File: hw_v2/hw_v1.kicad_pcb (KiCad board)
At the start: 4 copper layers, 80.6 x 93.7 mm, 179 parts, among them J1 Conn_02x24_Counter_Clockwise, J14 Conn_01x04, J16 47352-1001, J8 USB_B_Micro, J9 Tag connect, SW1 SW_Push, SW2 SW_Push, U1 MAX9924UAUB_, U10 BMP280, U11 L78M05ABDT-TR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

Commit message: wip CKP/CMP
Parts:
- removed C7: 0.01uF, Capacitor_SMD:C_0805_2012Metric
- removed C8: 4.7nF, Capacitor_SMD:C_0805_2012Metric
- removed the J8 at (115.3, 131.5)
- removed JP11, JP12: Jumper_2_Open, Jumper:SolderJumper-2_P1.3mm_Open_RoundedPad1.0x1.5mm
- removed TP1, TP4: TestPoint, TestPoint:TestPoint_Pad_1.0x1.0mm
- removed U18: VNLD5090, Package_SO:SOIC-8_3.9x4.9mm_P1.27mm
- added R12: 4.7K, Resistor_SMD:R_0603_1608Metric, F.Cu at (185.8, 103.0)
- added R13: 4.7K, Resistor_SMD:R_0603_1608Metric, F.Cu at (185.8, 105.5)
- added R14: 4.7K, Resistor_SMD:R_0603_1608Metric, F.Cu at (185.8, 108.0)
- added R15: 4.7K, Resistor_SMD:R_0603_1608Metric, F.Cu at (185.8, 110.5)
- added R5: 4.7K, Resistor_SMD:R_0603_1608Metric, F.Cu at (185.8, 93.0)
- added R6: 4.7K, Resistor_SMD:R_0603_1608Metric, F.Cu at (185.8, 95.5)
- added R8: 4.7K, Resistor_SMD:R_0603_1608Metric, F.Cu at (185.8, 98.0)
- added R9: 4.7K, Resistor_SMD:R_0603_1608Metric, F.Cu at (185.8, 100.5)
- added RN3: 47k, Resistor_SMD:R_Array_Convex_4x0603, F.Cu at (94.9, 119.8)
- added U2: ~, Package_SO:SOIC-8_3.9x4.9mm_P1.27mm, F.Cu at (131.3, 67.7)
- added U20: ~, Package_SO:SO-8_3.9x4.9mm_P1.27mm, B.Cu at (131.3, 67.7)
- added U3: ~, Package_SO:SOIC-8_3.9x4.9mm_P1.27mm, F.Cu at (138.3, 67.7)
- added U9: TPL7407LAPWR || ULN2003A, Package_SO:TSSOP-16_4.4x5mm_P0.65mm, F.Cu at (202.7, 113.7)
- C1, C2, C68, R2, R3, R7, TP5: moved to B.Cu
- D14, D16: footprint Package_TO_SOT_SMD:SOT-23-6 -> Package_TO_SOT_SMD:SOT-363_SC-70-6
- JP2: moved to F.Cu
- U13: value STM32F407VGTx -> ~; footprint Package_QFP:LQFP-100_14x14mm_P0.5mm -> Package_SO:SO-8_3.9x4.9mm_P1.27mm; moved to B.Cu
- U5: value TPL7407LAPWR -> ~; footprint Package_SO:TSSOP-16_4.4x5mm_P0.65mm -> Package_SO:SO-8_3.9x4.9mm_P1.27mm
- moved J8 151.8 mm to (114.5, 124.6)
- moved U22 139.7 mm to (105.0, 110.0), turned to -45 degrees
- moved U5 119.7 mm to (101.2, 77.2), turned to 90 degrees
- moved U17 102.3 mm to (115.3, 115.0), turned to -135 degrees
- moved R7 98.6 mm to (126.2, 64.8), turned to -90 degrees
- moved TP5 92.0 mm to (120.3, 70.4), turned to 180 degrees
- moved R11 88.9 mm to (119.5, 70.4)
- moved C2 86.5 mm to (123.7, 64.2), turned to -90 degrees
- moved R2 86.3 mm to (121.8, 63.9), turned to -90 degrees
- moved C1 85.7 mm to (122.1, 67.7), turned to -90 degrees
- moved R3 84.0 mm to (124.0, 67.4), turned to -90 degrees
- moved C5 83.3 mm to (125.8, 70.5), turned to -90 degrees
- moved JP3 83.2 mm to (126.1, 69.9), turned to 90 degrees
- moved D19 82.4 mm to (113.4, 117.8), turned to 135 degrees
- moved JP2 78.1 mm to (126.2, 66.4), turned to 90 degrees
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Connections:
- J1 pad 31: FUELPUMP-OUT -> FAN2-OUT
- J1 pad 32: TACHO-OUT -> FUELPUMP-OUT
- J1 pad 33: CAM+ -> TACHO-OUT
- J1 pad 34: unconnected-(J1-Pin_34-Pad34) -> CAM+
- R106 pad 1: /Sensors/AGND -> GND
- R108 pad 1: /Sensors/AGND -> GND
- R57 pad 2: Net-(U18-IN1) -> Net-(U5-IN1)
- R58 pad 1: Net-(U18-IN2) -> Net-(U5-IN2)
- U13 pad 1: /fan2 -> /INY1
- U13 pad 2: /vvt -> unconnected-(U13-STATUS1-Pad2)
- U13 pad 3: /boost -> /INY2
- U13 pad 4: /idle -> unconnected-(U13-STATUS2-Pad4)
- U13 pad 5: unconnected-(U13-PE6-Pad5) -> GND
- U13 pad 6: Net-(BT1-+) -> INJ-2-OUT
- U13 pad 7: 5V_ENABLE -> GND
- U13 pad 8: OSC32_IN -> INJ-1-OUT
- U24 pad 1: (no net) -> unconnected-(U24-Pad1)
- U24 pad 10: (no net) -> unconnected-(U24C-+-Pad10)
- U24 pad 2: (no net) -> unconnected-(U24A---Pad2)
- U24 pad 3: (no net) -> unconnected-(U24A-+-Pad3)
- U24 pad 8: (no net) -> unconnected-(U24-Pad8)
- U24 pad 9: (no net) -> unconnected-(U24C---Pad9)
- U5 pad 1: /fuel_pump -> Net-(U5-IN1)
- U5 pad 2: /fan1 -> unconnected-(U5-STATUS1-Pad2)
- U5 pad 3: /fan2 -> Net-(U5-IN2)
- U5 pad 4: /RPM_OUT -> unconnected-(U5-STATUS2-Pad4)
- U5 pad 5: /RPM_OUT -> GND
- U5 pad 6: /CEL_OUT -> BOOST-OUT
- U5 pad 7: /CEL_OUT -> GND
- U5 pad 8: GND -> IDLE-OUT
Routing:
- net USB_D+: track 0.00 -> 78.4 mm, vias 0 -> 1
- net USB_D-: track 0.00 -> 76.7 mm, vias 0 -> 1
- net GND: track 12.5 -> 32.1 mm, vias 8 -> 14
- net /MAP: track 1.94 -> 17.2 mm
- net /CKP_CMP_Sensors/IN2-: track 0.00 -> 14.3 mm, vias 0 -> 1
- net /IAT: track 2.86 -> 16.3 mm
- net /CLT: track 3.31 -> 16.5 mm
- net VBUS: track 0.00 -> 13.0 mm
- net /TPS: track 2.15 -> 15.1 mm
- net CRANK+: track 0.00 -> 11.1 mm
- net /CKP_CMP_Sensors/IN2+: track 0.00 -> 10.5 mm, vias 0 -> 1
- net +3V3: track 6.93 -> 13.5 mm, vias 0 -> 2
- net Net-(U22-VCAP_2): track 0.00 -> 4.97 mm
- net Net-(U13-VCAP_2): track 4.95 -> 0.00 mm
- net /CKP_CMP_Sensors/CKP_VR: track 0.00 -> 4.66 mm, vias 0 -> 1
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
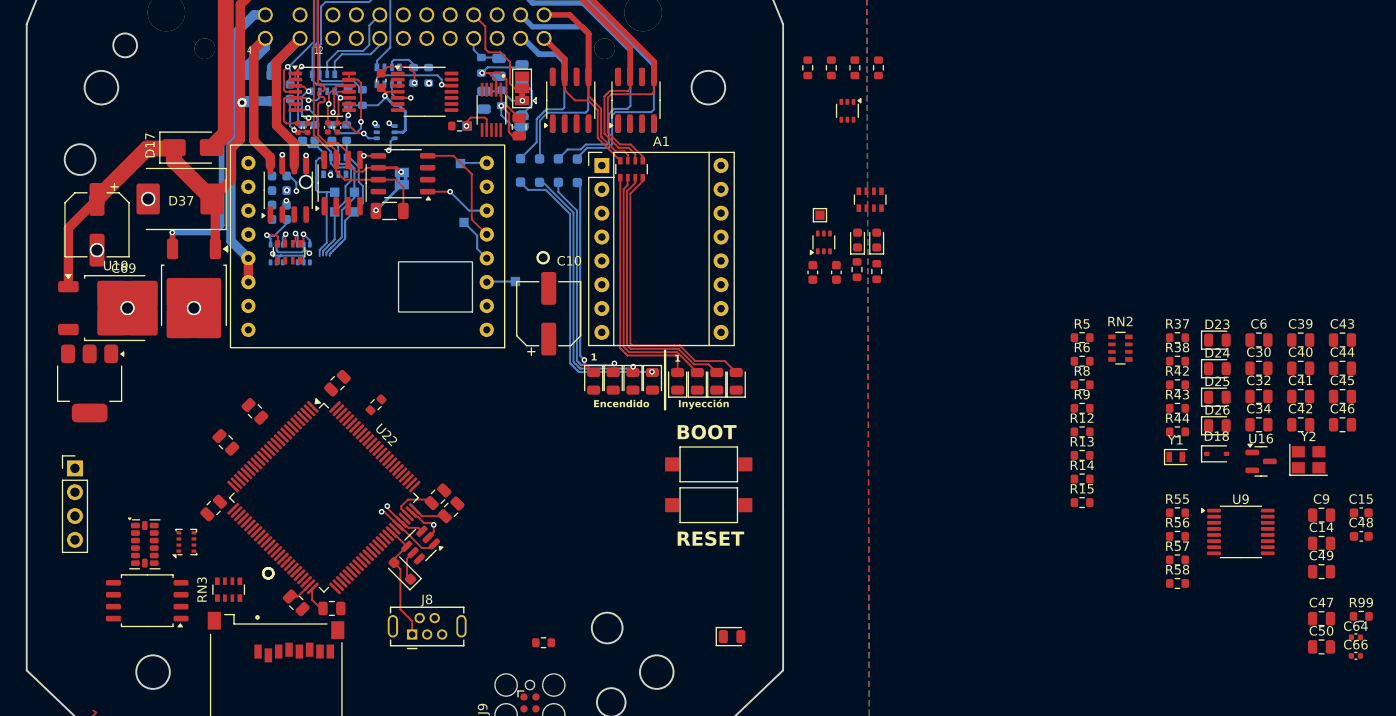
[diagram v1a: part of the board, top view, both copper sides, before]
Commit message: wip routing iny/ign drivers
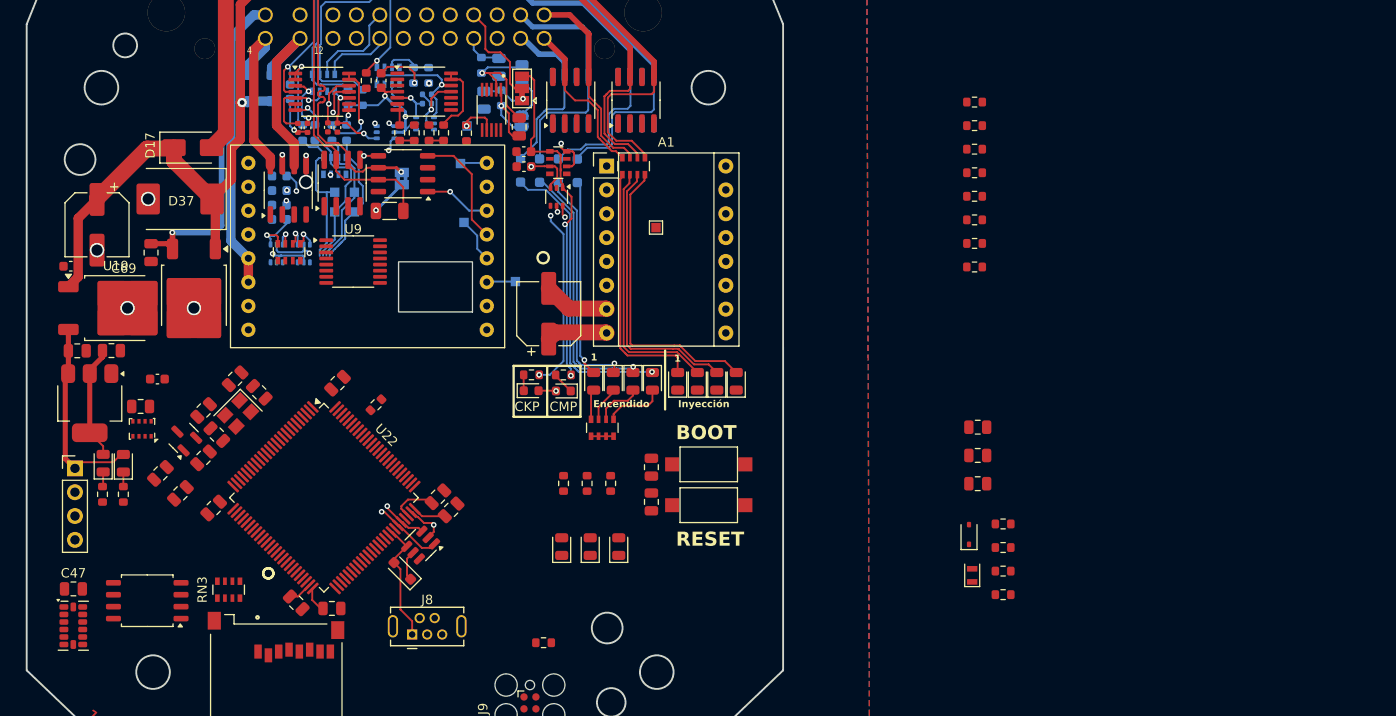
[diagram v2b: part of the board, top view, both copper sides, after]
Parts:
- removed C32: 100nF, Capacitor_SMD:C_0805_2012Metric
- removed C34: 1uF, Capacitor_SMD:C_0805_2012Metric
- C64, C66, D16: moved to B.Cu
- moved C15 140.0 mm to (78.1, 85.3), turned to 180 degrees
- moved C49 134.6 mm to (78.8, 94.3)
- moved C47 133.0 mm to (78.4, 119.7)
- moved C9 130.1 mm to (82.4, 94.3)
- moved C48 129.4 mm to (87.3, 97.4)
- moved C14 128.5 mm to (86.6, 83.9), turned to -90 degrees
- moved C50 128.4 mm to (85.5, 100.3), turned to 180 degrees
- moved C46 126.0 mm to (87.6, 107.4), turned to -135 degrees
- moved C45 124.2 mm to (89.8, 109.5), turned to -135 degrees
- moved C44 121.7 mm to (92.2, 105.8), turned to 45 degrees
- moved R99 120.4 mm to (109.6, 65.6), turned to -90 degrees
- moved C43 120.4 mm to (93.6, 103.3), turned to 135 degrees
- moved D23 119.4 mm to (81.5, 106.3), turned to 90 degrees
- moved R38 115.4 mm to (81.5, 109.6), turned to -90 degrees
- moved C66 115.1 mm to (116.0, 68.0)
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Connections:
- D16 pad 1: unconnected-(D16-Pad1) -> Net-(RN6-R1.2)
- D16 pad 3: Net-(RN6-R1.2) -> unconnected-(D16-Pad3)
- J1 pad 37: STEPPER-B2 -> STEPPER-A2
- J1 pad 38: STEPPER-B1 -> STEPPER-A1
- J1 pad 39: STEPPER-A2 -> STEPPER-B1
- J1 pad 40: STEPPER-A1 -> STEPPER-B2
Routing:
- net +5C: track 90.4 -> 145.6 mm, vias 3 -> 7
- net CAM+: track 0.00 -> 52.3 mm, vias 0 -> 3
- net Net-(JP2-B): track 0.00 -> 37.3 mm, vias 0 -> 2
- net STEPPER-A2: track 0.00 -> 34.4 mm
- net STEPPER-A1: track 0.00 -> 33.2 mm
- net STEPPER-B1: track 0.00 -> 32.4 mm
- net STEPPER-B2: track 0.00 -> 31.4 mm
- net /CKP: track 4.09 -> 25.4 mm, vias 1 -> 2
- net +5V: track 3.26 -> 24.4 mm
- net GND: track 32.1 -> 47.3 mm, vias 14 -> 15
- net +3V3: track 13.5 -> 25.7 mm
- net HEATER+: track 86.8 -> 95.7 mm
- net Net-(U24D--): track 0.00 -> 7.87 mm
- net Net-(D2-A): track 0.00 -> 6.45 mm
- net Net-(D5-A): track 0.00 -> 5.17 mm
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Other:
- board text added: "CKP"
- board text added: "CMP"

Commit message: wip mcu routing
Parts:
- removed JP10, JP9: SolderJumper_3_Bridged12, Jumper:SolderJumper-3_P1.3mm_Bridged2Bar12_Pad1.0x1.5mm
- C40, C41, TP19, U9, Y1: moved to B.Cu
- JP13, JP6, JP7, JP8: moved to F.Cu
- moved JP8 102.2 mm to (144.7, 84.7), turned to 0 degrees
- moved JP6 102.0 mm to (144.7, 89.9), turned to 0 degrees
- moved JP7 101.9 mm to (144.7, 87.3), turned to 0 degrees
- moved C39 90.1 mm to (86.3, 119.9)
- moved R57 84.1 mm to (99.1, 87.2), turned to 90 degrees
- moved D18 83.2 mm to (180.8, 31.0), turned to 0 degrees
- moved R58 82.2 mm to (102.2, 87.2), turned to -90 degrees
- moved R56 81.8 mm to (100.7, 87.2), turned to 90 degrees
- moved C41 79.1 mm to (96.0, 100.8), turned to 135 degrees
- moved Y1 78.7 mm to (97.7, 99.7), turned to -45 degrees
- moved R55 78.0 mm to (103.8, 87.2), turned to -90 degrees
- moved JP13 77.1 mm to (126.2, 77.9), turned to 90 degrees
- moved C40 76.3 mm to (98.8, 98.0), turned to 135 degrees
- moved TP7 68.4 mm to (104.2, 109.4)
- moved TP8 66.4 mm to (102.2, 112.7)
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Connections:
- J1 pad 23: LSU_ip -> LSU_un
- J1 pad 24: LSU_vm -> LSU_rtrim
- J1 pad 25: LSU_rtrim -> unconnected-(J1-Pin_25-Pad25)
- J1 pad 26: LSU_un -> unconnected-(J1-Pin_26-Pad26)
- J1 pad 27: unconnected-(J1-Pin_27-Pad27) -> LSU_vm
- J1 pad 28: unconnected-(J1-Pin_28-Pad28) -> LSU_ip
- J14 pad 3: Net-(J14-Pin_3) -> USART_2_RX
- J14 pad 4: Net-(J14-Pin_4) -> USART_2_TX
- U22 pad 1: /fan1 -> /fan2
- U22 pad 15: /CEL_OUT -> unconnected-(U22-PC0-Pad15)
- U22 pad 2: /fuel_pump -> /fan1
- U22 pad 23: /IAT -> /CLT
- U22 pad 26: /CLT -> /IAT
- U22 pad 3: /fan2 -> /fuel_pump
- U22 pad 42: /RPM_OUT -> unconnected-(U22-PE11-Pad42)
- U22 pad 92: unconnected-(U22-PB6-Pad92) -> /RPM_OUT
- U22 pad 93: unconnected-(U22-PB7-Pad93) -> /CEL_OUT
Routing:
- net /O2: track 1.55 -> 54.5 mm, vias 0 -> 2
- net /VBATT: track 1.55 -> 51.8 mm, vias 0 -> 2
- net IGN_V+: track 0.00 -> 39.0 mm, vias 0 -> 3
- net LSU_vm: track 0.00 -> 37.0 mm
- net LSU_ip: track 0.00 -> 36.9 mm
- net /MAP: track 17.2 -> 52.9 mm, vias 0 -> 1
- net /TPS: track 15.1 -> 50.4 mm, vias 0 -> 1
- net /IAT: track 16.3 -> 51.6 mm, vias 0 -> 1
- net /fuel_pump: track 0.00 -> 33.1 mm, vias 0 -> 1
- net /fan1: track 0.00 -> 32.3 mm, vias 0 -> 1
- net /fan2: track 0.00 -> 31.6 mm, vias 0 -> 1
- net FAN-OUT: track 0.00 -> 31.1 mm, vias 0 -> 2
- net LSU_rtrim: track 0.00 -> 30.7 mm
- net /CLT: track 16.5 -> 47.1 mm, vias 0 -> 1
- net TACHO-OUT: track 0.00 -> 30.5 mm, vias 0 -> 2
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
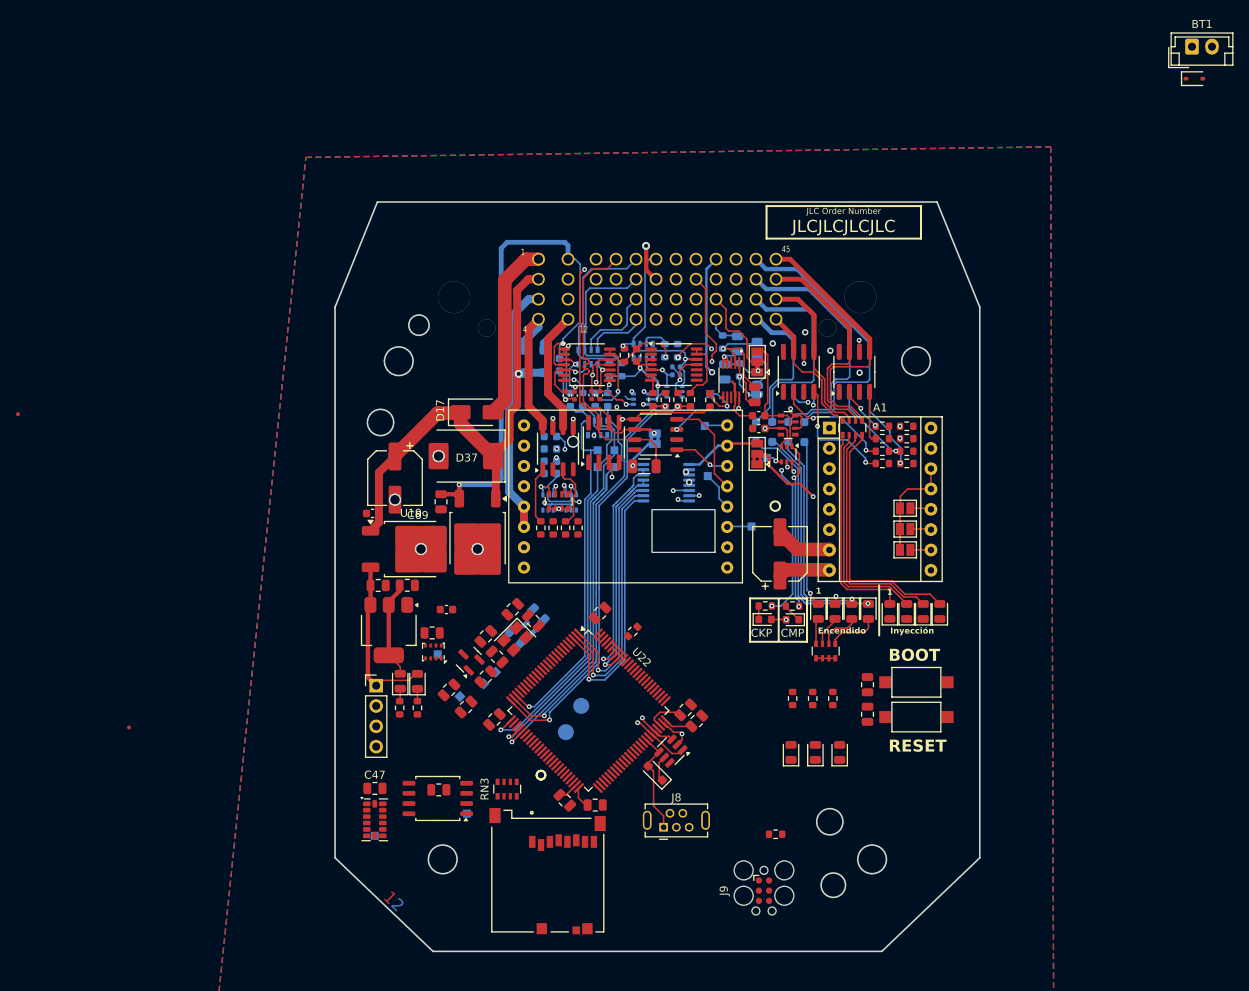
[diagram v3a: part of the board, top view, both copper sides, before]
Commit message: update ADC oamp
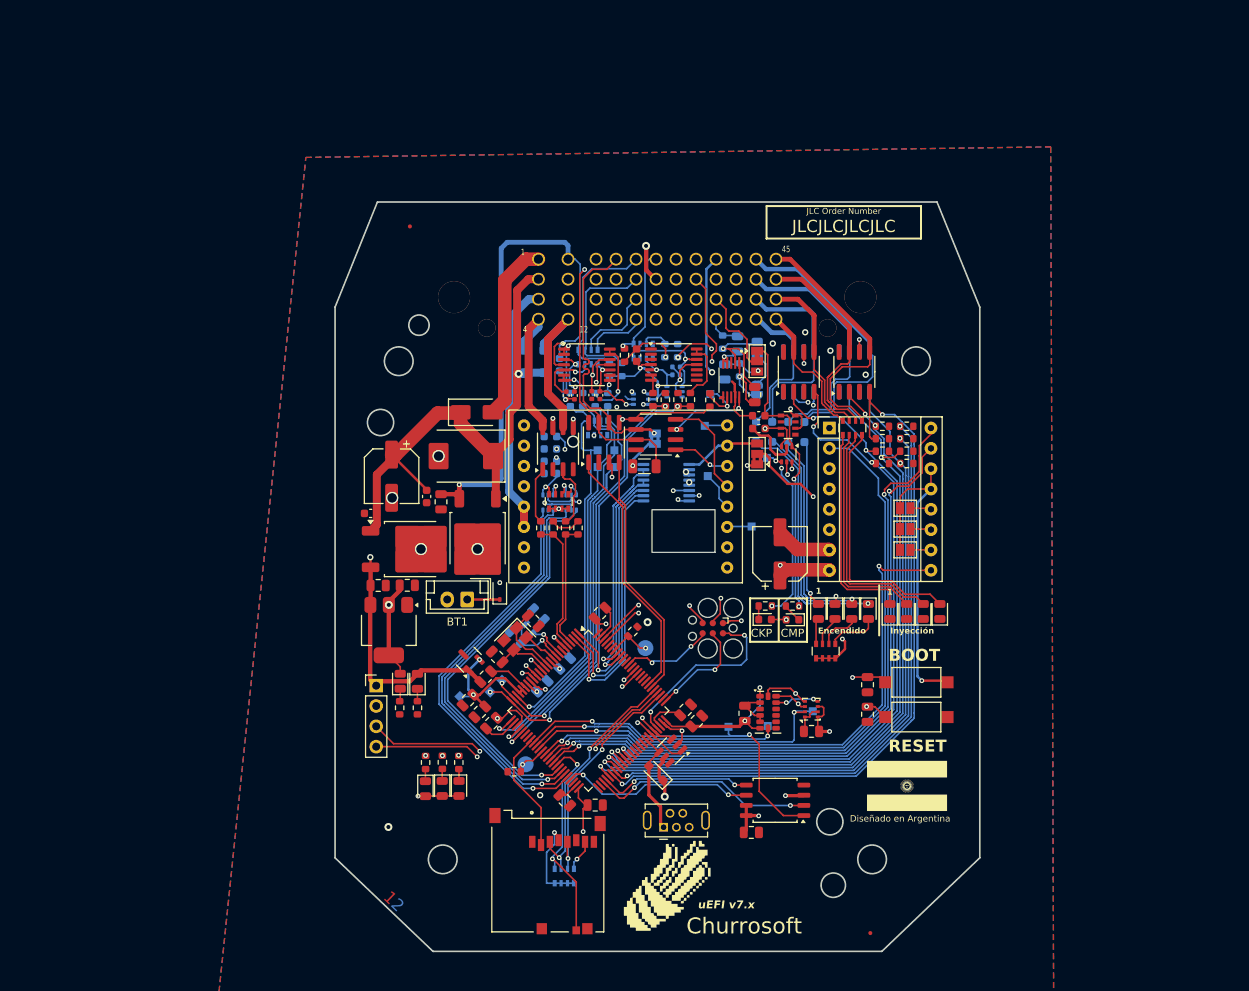
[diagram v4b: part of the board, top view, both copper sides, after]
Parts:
- removed the G*** at (142.0, 115.0)
- added Churrosoft: SYM_Hot_Large, OpenEFI-STM32F_rev3:churro_new_v4, F.Cu at (115.1, 131.9)
- added G***: LOGO, LOGO, F.Cu at (144.9, 119.4)
- added G***: LOGO, LOGO, B.Cu at (144.4, 102.8)
- added G***: LOGO, LOGO, B.Cu at (141.4, 115.3)
- C37, C38, RN3: moved to B.Cu
- U6: footprint Package_SO:SOP-8_3.9x4.9mm_P1.27mm -> Package_SO:SOIC-8_3.9x4.9mm_P1.27mm
- moved BT1 113.9 mm to (89.9, 96.1), turned to 180 degrees
- moved D18 107.9 mm to (94.0, 95.0), turned to 90 degrees
- moved FID2 96.2 mm to (140.3, 137.8)
- moved FID1 54.3 mm to (82.7, 49.5)
- moved TP17 51.0 mm to (127.5, 111.9)
- moved U21 51.0 mm to (127.5, 110.2)
- moved C50 49.0 mm to (132.9, 112.6)
- moved D26 47.8 mm to (88.9, 119.7), turned to -90 degrees
- moved U10 47.8 mm to (132.9, 109.8), turned to 90 degrees
- moved R44 47.4 mm to (88.8, 116.5)
- moved TP18 47.4 mm to (133.1, 110.1), turned to -90 degrees
- moved C47 47.2 mm to (124.6, 110.3), turned to 90 degrees
- moved R43 47.0 mm to (86.8, 116.5)
- moved D25 46.9 mm to (86.8, 119.7), turned to -90 degrees
- moved R42 46.6 mm to (84.7, 116.5)
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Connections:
- C3 pad 1: Net-(JP2-B) -> Net-(JP2-A)
- JP2 pad 1: /CKP_CMP_Sensors/CKP_VR -> Net-(JP2-A)
- JP2 pad 3: Net-(JP2-B) -> /CKP_CMP_Sensors/CKP_VR
- R1 pad 1: Net-(JP2-B) -> Net-(JP2-A)
- RN3 pad 3: /SPI3_MISO -> /SPI3_SCk
- RN3 pad 4: /SPI3_SCk -> /SPI3_MISO
- RN5 pad 5: Net-(JP2-B) -> Net-(JP2-A)
- U22 pad 33: unconnected-(U22-PC4-Pad33) -> /SD_CS
- U22 pad 34: unconnected-(U22-PC5-Pad34) -> /MEMORY_CS
- U22 pad 35: unconnected-(U22-PB0-Pad35) -> ACCL_CS
- U22 pad 36: unconnected-(U22-PB1-Pad36) -> BARO_CS
- U22 pad 38: /MTR_STEP -> /MTR_ENABLE
- U22 pad 39: /MTR_DIR -> /MTR_FAULT
- U22 pad 40: /MTR_FAULT -> /MTR_DIR
- U22 pad 41: /MTR_ENABLE -> /MTR_STEP
- U22 pad 42: unconnected-(U22-PE11-Pad42) -> /SD_CARD_DETECT
- U22 pad 43: /SW_AC_m -> /SW_TABLE_m
- U22 pad 45: /SW_TABLE_m -> /SW_AC_m
- U22 pad 52: /MEMORY_CS -> unconnected-(U22-PB13-Pad52)
- U22 pad 55: /INY1 -> /INY3
- U22 pad 56: /INY2 -> /ECN3
- U22 pad 57: /INY3 -> /INY4
- U22 pad 58: /INY4 -> /INY1
- U22 pad 59: /ECN1 -> /ECN4
- U22 pad 60: /ECN2 -> /INY2
- U22 pad 61: /ECN3 -> /ECN2
- U22 pad 62: /ECN4 -> /ECN1
- U22 pad 65: /SD_CS -> unconnected-(U22-PC8-Pad65)
- U22 pad 66: /SD_CARD_DETECT -> unconnected-(U22-PC9-Pad66)
- U22 pad 83: /SD_CS -> unconnected-(U22-PD2-Pad83)
- U22 pad 95: ACCL_CS -> unconnected-(U22-PB8-Pad95)
- U22 pad 96: BARO_CS -> unconnected-(U22-PB9-Pad96)
- U7 pad 1: Net-(JP2-B) -> Net-(JP2-A)
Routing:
- net +3V3: track 49.2 -> 355.4 mm, vias 2 -> 18
- net HEATER+: track 99.3 -> 239.5 mm, vias 3 -> 5
- net +5V: track 48.0 -> 171.1 mm, vias 3 -> 6
- net /ECN3: track 6.51 -> 92.2 mm, vias 0 -> 2
- net /MTR_DIR: track 0.00 -> 84.6 mm, vias 0 -> 2
- net /MTR_FAULT: track 0.00 -> 82.4 mm, vias 0 -> 1
- net /MTR_STEP: track 0.00 -> 82.0 mm, vias 0 -> 2
- net /ECN4: track 5.70 -> 84.8 mm, vias 2 -> 3
- net /INY3: track 14.2 -> 92.6 mm, vias 2 -> 3
- net /INY4: track 16.0 -> 93.5 mm, vias 2 -> 3
- net /INY2: track 10.5 -> 86.6 mm, vias 1 -> 2
- net /INY1: track 10.5 -> 85.0 mm, vias 1 -> 2
- net /ECN2: track 14.9 -> 88.5 mm, vias 2 -> 3
- net /ECN1: track 14.8 -> 85.0 mm, vias 2 -> 3
- net /MTR_ENABLE: track 0.00 -> 69.9 mm, vias 0 -> 2
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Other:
- board text added: "Diseñado en Argentina"
- board text added: "uEFI v7.x"
- board text removed: "GND"
- board text removed: "J5"
